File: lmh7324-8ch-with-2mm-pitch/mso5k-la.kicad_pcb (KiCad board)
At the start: 4 copper layers, 40 x 44 mm, 101 parts, among them IC201 lmh7324, IC401 lmh7324, J101 out, J102 in, J103 3mm, J104 3mm, J105 3mm, J106 3mm, U401 ATtiny85-20SU

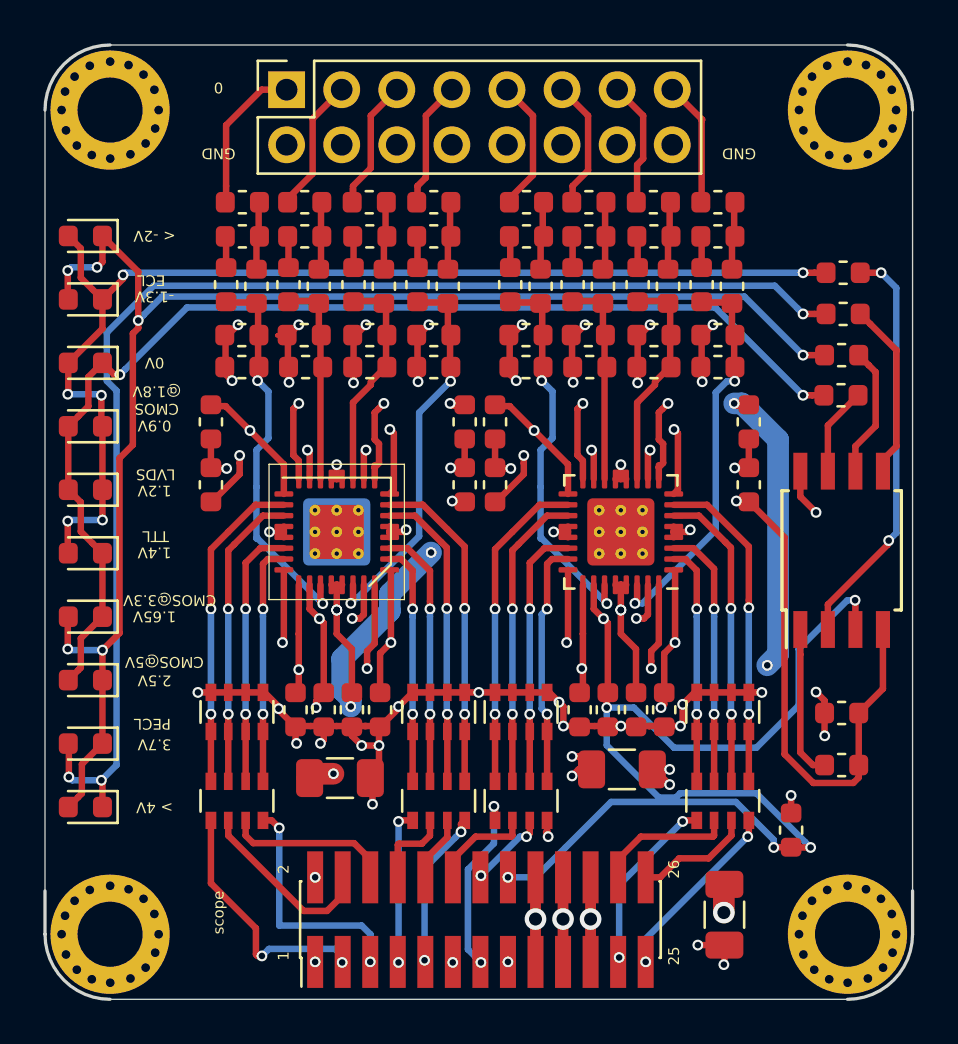
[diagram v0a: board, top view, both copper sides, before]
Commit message: Switched to an SMD 1.27 mm pitch header for the cable to the scope to get a thinner uplink ribbon
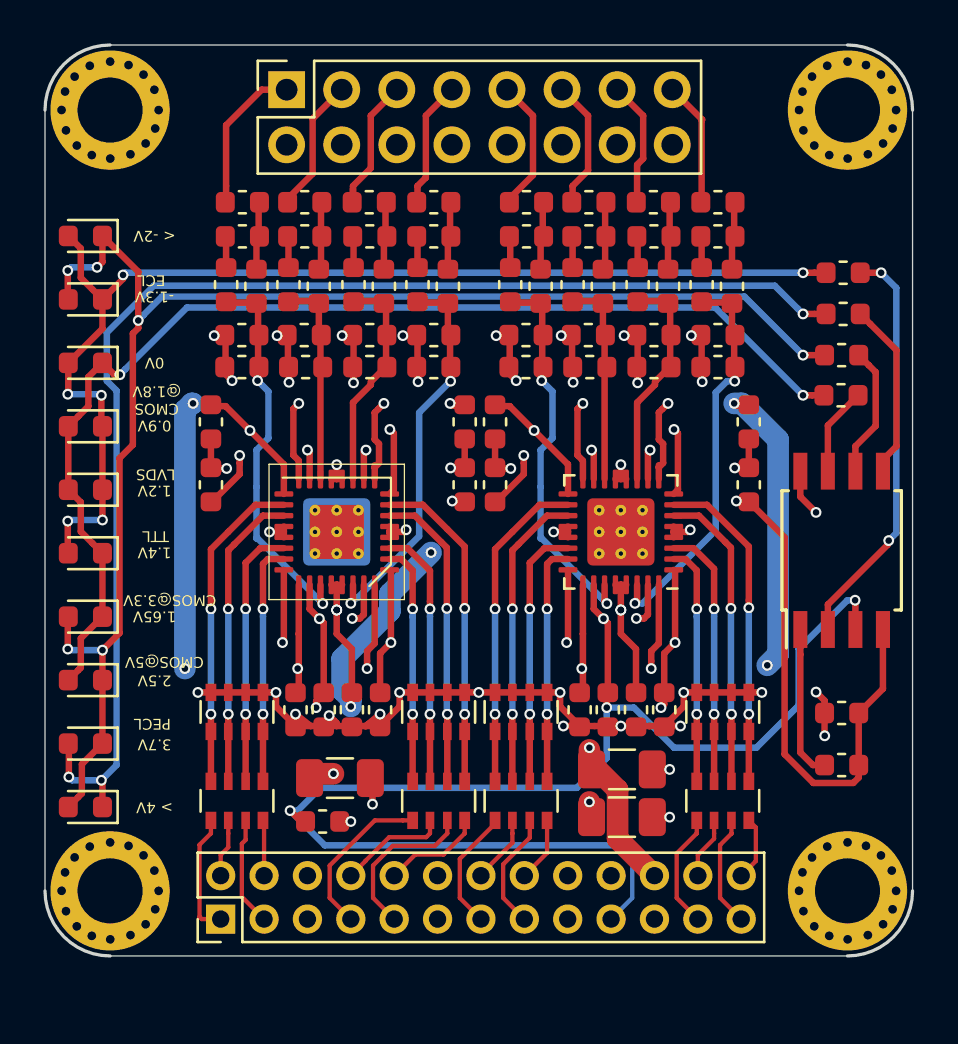
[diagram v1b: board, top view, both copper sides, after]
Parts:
- J101: footprint Connector_PinHeader_1.27mm:PinHeader_2x13_P1.27mm_Vertical_SMD -> Connector_PinHeader_2.00mm:PinHeader_2x13_P2.00mm_Vertical
- moved C104 21.6 mm to (57.8, 180.8), turned to 0 degrees
- moved J101 12.0 mm to (53.1, 185.3)
- moved C102 6.53 mm to (71.6, 180.6), turned to 0 degrees
- moved J104 2.00 mm to (48.0, 184.0)
- moved J106 2.00 mm to (82.0, 184.0)
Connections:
- J101 pad 1: GND -> D1-
- J101 pad 10: D2+ -> D2-
- J101 pad 11: D4- -> GND
- J101 pad 12: D5+ -> GND
- J101 pad 14: D4+ -> D5+
- J101 pad 15: GND -> D4+
- J101 pad 16: Vref -> D4-
- J101 pad 17: -2V5 -> GND
- J101 pad 19: +2V5 -> Vref
- J101 pad 2: GND -> D1+
- J101 pad 21: +4V -> GND
- J101 pad 25: D6- -> D6+
- J101 pad 26: D6+ -> D6-
- J101 pad 3: D1- -> D0+
- J101 pad 4: D1+ -> D0-
- J101 pad 5: D0- -> GND
- J101 pad 6: D0+ -> GND
- J101 pad 9: D2- -> D2+
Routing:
- net GND: track 272.3 -> 290.5 mm, vias 43 -> 37
- net +2V5: track 155.2 -> 139.6 mm, vias 14 -> 13
- net +4V: track 108.2 -> 123.6 mm
- net D0-: track 12.3 -> 2.57 mm, vias 2 -> 0
- net Vref: track 144.4 -> 153.5 mm, vias 16 -> 14
- net -2V5: track 127.7 -> 120.9 mm, vias 16 -> 15
- net D1-: track 11.9 -> 5.68 mm, vias 2 -> 0
- net D4-: track 9.16 -> 2.98 mm, vias 2 -> 0
- net D6-: track 8.81 -> 2.96 mm, vias 2 -> 0
- net D1+: track 8.54 -> 2.69 mm
- net D2+: track 3.05 -> 7.51 mm
- net D7+: track 6.41 -> 2.86 mm
- net D7-: track 8.38 -> 5.34 mm, vias 2 -> 0
- net D5-: track 8.65 -> 5.63 mm, vias 2 -> 0
- net D0+: track 7.73 -> 5.05 mm
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- removed copper zone on 3_Misc, net +4V
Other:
- board size 40 x 44 mm -> 40 x 42 mm
- board text removed: "0"
- board text removed: "1"
- board text removed: "2"
- board text removed: "25"
- board text removed: "26"
- board text removed: "GND"
- board text removed: "scope"
